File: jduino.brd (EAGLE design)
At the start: 58.1 x 66 mm, 18 parts, among them IC1 LM2936Z-5.0, IC2 ATMEGA48/88/168-PU, J1 Analog I/O, J2 Digital I/O, J3 Digital I/O, J5 Power Jumpers, J6 FTDI Jumpers, Q1 16 mHz

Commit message: Final fixes for printing.
Replaced power IC with 2931. Added an LED on pin 13.
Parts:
- added LED2: LED 13, led:LED3MM
- added R3: 330, rcl:0204/5
- IC1: value LM2936Z-5.0 -> L4931; device national-semiconductor:TO92 -> jb:TO-92
- J7: value (none) -> POWER 6 - 36V
- moved IC1 1.27 mm to (33.0, 58.4), flipped to the top, turned to 180 degrees
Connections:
- removed net D1: IC2.3, J2.2, J6.2
- new net N$4: LED2.K, R3.2
- net D13: now also LED2.A
- net GND: now also R3.1
- net RESET: now also IC2.3, J2.2, J6.2
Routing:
- net D1: track 35.9 -> 0.00 mm, vias 2 -> 0
- net RESET: track 74.6 -> 107.8 mm, vias 4 -> 6
- net GND: track 223.9 -> 234.1 mm
- net D7: track 28.1 -> 33.1 mm
- net D6: track 28.1 -> 32.6 mm
- net D5: track 28.1 -> 32.6 mm
- net +5V: track 152.1 -> 156.0 mm
- net D9: track 36.3 -> 37.5 mm
- net D8: track 27.6 -> 28.9 mm
- net D13: track 59.1 -> 60.4 mm
- net D12: track 54.0 -> 55.3 mm
- net D10: track 43.9 -> 45.2 mm
- net D11: track 49.0 -> 50.2 mm
- net N$6: track 8.15 -> 6.88 mm

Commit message: Small fixes to the circuit.
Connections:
- new net D1: IC2.3, J2.2, J6.2
- net RESET: no longer IC2.3, J2.2, J6.2
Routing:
- net RESET: track 107.8 -> 71.9 mm, vias 6 -> 4
- net D1: track 0.00 -> 35.9 mm, vias 0 -> 2
- net N$4: track 0.00 -> 2.54 mm
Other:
- board text added: "jduino v1.0"
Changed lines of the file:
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@@
 <drawing>
 <settings>
-<setting alwaysvectorfont="no"/>
+<setting alwaysvectorfont="yes"/>
 <setting verticaltext="up"/>
 </settings>
-<grid distance="0.05" unitdist="inch" unit="inch" style="lines" multiple="1" display="yes" altdistance="0.025" altunitdist="inch" altunit="inch"/>
+<grid distance="0.05" unitdist="inch" unit="mm" style="lines" multiple="1" display="yes" altdistance="0.025" altunitdist="inch" altunit="inch"/>
 <layers>
-<layer number="1" name="Top" color="4" fill="1" visible="no" active="yes"/>
+<layer number="1" name="Top" color="4" fill="1" visible="yes" active="yes"/>
 <layer number="16" name="Bottom" color="1" fill="1" visible="yes" active="yes"/>
 <layer number="17" name="Pads" color="2" fill="1" visible="yes" active="yes"/>
 <layer number="18" name="Vias" color="2" fill="1" visible="yes" active="yes"/>
-<layer number="19" name="Unrouted" color="6" fill="1" visible="no" active="yes"/>
+<layer number="19" name="Unrouted" color="6" fill="1" visible="yes" active="yes"/>
 <layer number="20" name="Dimension" color="15" fill="1" visible="yes" active="yes"/>
 <layer number="21" name="tPlace" color="16" fill="1" visible="no" active="yes"/>
@@
 <layer number="106" name="bPlate" color="7" fill="1" visible="no" active="yes"/>
 <layer number="107" name="Crop" color="7" fill="1" visible="no" active="yes"/>
-<layer number="116" name="Patch_BOT" color="9" fill="4" visible="no" active="yes"/>
+<layer number="116" name="centerDrill" color="7" fill="1" visible="yes" active="yes"/>
 <layer number="121" name="_tsilk" color="7" fill="1" visible="no" active="yes"/>
 <layer number="122" name="_bsilk" color="7" fill="1" visible="no" active="yes"/>
@@
 <wire x1="58.09" y1="66.03" x2="0" y2="66.03" width="0" layer="20"/>
 <wire x1="0" y1="66.03" x2="0" y2="0" width="0" layer="20"/>
+<text x="13.335" y="47.625" size="1.016" layer="16" ratio="10" rot="MR0">jduino v1.0</text>
 </plain>
 <attributes>
@@
 <wire x1="45.72" y1="2.54" x2="15.24" y2="2.54" width="0.6096" layer="16"/>
 <wire x1="15.24" y1="2.54" x2="7.62" y2="10.16" width="0.6096" layer="16"/>
-<polygon width="0.6096" layer="16">
+<polygon width="0.25" layer="16">
 <vertex x="1.27" y="1.27"/>
+<vertex x="57.15" y="1.27"/>
+<vertex x="57.15" y="64.77"/>
 <vertex x="1.27" y="64.77"/>
-<vertex x="57.15" y="64.77"/>
-<vertex x="57.15" y="1.27"/>
 </polygon>
 </signal>
@@
 <contactref element="RESET" pad="4"/>
 <contactref element="C4" pad="1"/>
-<contactref element="J5" pad="1"/>
 <wire x1="30.48" y1="13.97" x2="34.29" y2="13.97" width="0.4064" layer="16"/>
 <wire x1="29.21" y1="10.16" x2="30.48" y2="11.43" width="0.4064" layer="16"/>
@@
 <wire x1="12.7" y1="11.43" x2="11.43" y2="11.43" width="0.4064" layer="16"/>
 <wire x1="11.43" y1="11.43" x2="9.8806" y2="10.8712" width="0.4064" layer="16"/>
-<wire x1="29.21" y1="10.16" x2="30.48" y2="8.89" width="0.4064" layer="16"/>
-<wire x1="30.48" y1="8.89" x2="30.48" y2="7.62" width="0.4064" layer="16"/>
 <wire x1="30.48" y1="7.62" x2="22.86" y2="7.62" width="0.4064" layer="1"/>
 <wire x1="22.86" y1="7.62" x2="19.05" y2="11.43" width="0.4064" layer="16"/>
@@
 <via x="30.48" y="7.62" extent="1-16" drill="0.9" shape="square"/>
 <via x="22.86" y="7.62" extent="1-16" drill="0.9" shape="square"/>
-<contactref element="J6" pad="2"/>
-<contactref element="IC2" pad="3"/>
-<contactref element="J2" pad="2"/>
-<wire x1="30.48" y1="19.05" x2="43.18" y2="19.05" width="0.4064" layer="16"/>
-<wire x1="43.18" y1="19.05" x2="45.72" y2="19.05" width="0.4064" layer="16"/>
-<wire x1="45.72" y1="19.05" x2="48.26" y2="16.51" width="0.4064" layer="16"/>
-<wire x1="48.26" y1="16.51" x2="53.34" y2="16.51" width="0.4064" layer="16"/>
-<wire x1="41.91" y1="7.62" x2="41.91" y2="11.43" width="0.4064" layer="16"/>
-<wire x1="41.91" y1="11.43" x2="43.18" y2="12.7" width="0.4064" layer="16"/>
-<wire x1="43.18" y1="12.7" x2="43.18" y2="19.05" width="0.4064" layer="1"/>
-<via x="43.18" y="12.7" extent="1-16" drill="1" shape="square"/>
-<via x="43.18" y="19.05" extent="1-16" drill="1" shape="square"/>
-<wire x1="8.89" y1="44.45" x2="5.08" y2="44.45" width="0.4064" layer="16"/>
-<wire x1="30.48" y1="13.97" x2="30.48" y2="19.05" width="0" layer="19" extent="1-1"/>
+<wire x1="30.48" y1="7.62" x2="30.48" y2="8.89" width="0.4" layer="16"/>
+<wire x1="30.48" y1="8.89" x2="29.21" y2="10.16" width="0.4" layer="16"/>
+<contactref element="J5" pad="1"/>
+<wire x1="5.08" y1="44.45" x2="8.89" y2="44.45" width="0.4" layer="16"/>
 </signal>
 <signal name="A0">
@@
 <contactref element="J1" pad="4"/>
 <contactref element="IC2" pad="26"/>
-<wire x1="5.08" y1="19.05" x2="22.86" y2="19.05" width="0.4064" layer="16"/>
+<wire x1="5.08" y1="19.05" x2="22.86" y2="19.05" width="0.4" layer="16"/>
 </signal>
 <signal name="A4">
@@
 <contactref element="LED2" pad="K"/>
 <contactref element="R3" pad="2"/>
-<wire x1="39.37" y1="54.61" x2="41.91" y2="54.61" width="0" layer="19" extent="1-1"/>
+<wire x1="39.37" y1="54.61" x2="41.91" y2="54.61" width="0.4" layer="16"/>
+</signal>
+<signal name="D1">
+<contactref element="J6" pad="2"/>
+<contactref element="IC2" pad="3"/>
+<contactref element="J2" pad="2"/>
+<wire x1="30.48" y1="19.05" x2="43.18" y2="19.05" width="0.4064" layer="16"/>
+<wire x1="43.18" y1="19.05" x2="45.72" y2="19.05" width="0.4064" layer="16"/>
+<wire x1="45.72" y1="19.05" x2="48.26" y2="16.51" width="0.4064" layer="16"/>
+<wire x1="48.26" y1="16.51" x2="53.34" y2="16.51" width="0.4064" layer="16"/>
+<wire x1="41.91" y1="7.62" x2="41.91" y2="11.43" width="0.4064" layer="16"/>
+<wire x1="41.91" y1="11.43" x2="43.18" y2="12.7" width="0.4064" layer="16"/>
+<wire x1="43.18" y1="12.7" x2="43.18" y2="19.05" width="0.4064" layer="1"/>
+<via x="43.18" y="12.7" extent="1-16" drill="1" shape="square"/>
+<via x="43.18" y="19.05" extent="1-16" drill="1" shape="square"/>
 </signal>
 </signals>

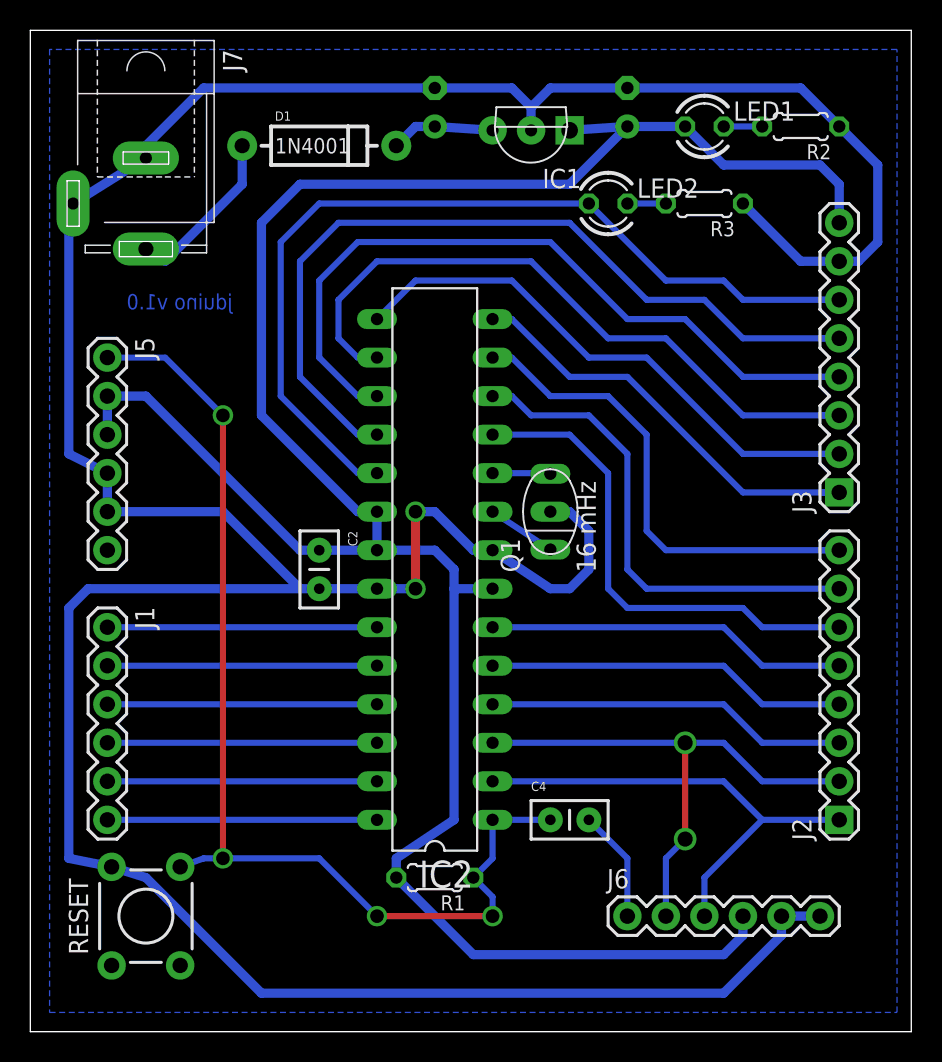
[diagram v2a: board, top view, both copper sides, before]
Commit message: Cleaned up area around reset button.
Rotated the reset button. Tied extra button terminals to the live
terminals.
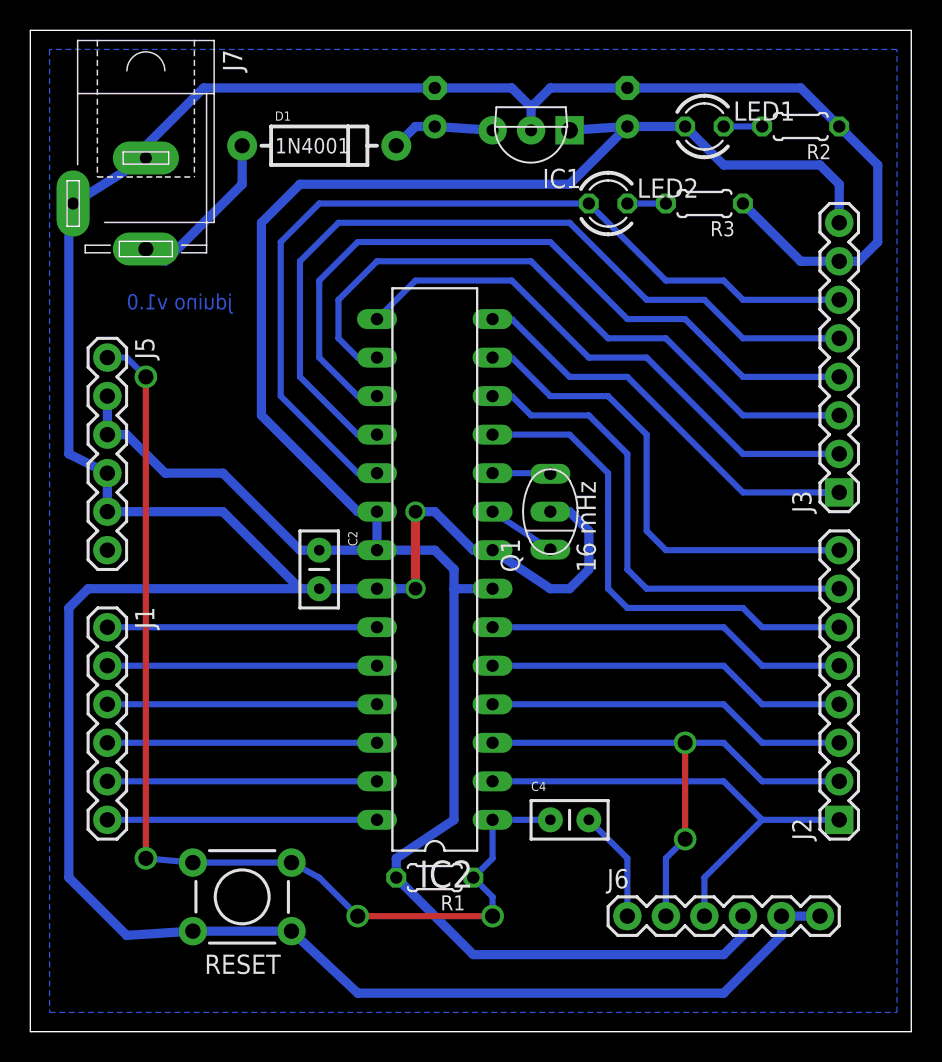
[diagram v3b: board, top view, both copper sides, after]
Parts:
- moved RESET 6.48 mm to (14.0, 8.89), turned to 180 degrees
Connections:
- net GND: now also RESET.1
- net RESET: now also RESET.3
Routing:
- net RESET: track 71.9 -> 70.2 mm
- net GND: track 234.1 -> 235.2 mm
- net +5V: track 156.0 -> 154.9 mm
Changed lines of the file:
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@@
 <setting verticaltext="up"/>
 </settings>
-<grid distance="0.05" unitdist="inch" unit="mm" style="lines" multiple="1" display="yes" altdistance="0.025" altunitdist="inch" altunit="inch"/>
+<grid distance="50" unitdist="mil" unit="mil" style="lines" multiple="1" display="yes" altdistance="25" altunitdist="mil" altunit="mil"/>
 <layers>
 <layer number="1" name="Top" color="4" fill="1" visible="yes" active="yes"/>
@@
 <layer number="19" name="Unrouted" color="6" fill="1" visible="yes" active="yes"/>
 <layer number="20" name="Dimension" color="15" fill="1" visible="yes" active="yes"/>
-<layer number="21" name="tPlace" color="16" fill="1" visible="no" active="yes"/>
+<layer number="21" name="tPlace" color="16" fill="1" visible="yes" active="yes"/>
 <layer number="22" name="bPlace" color="14" fill="1" visible="no" active="yes"/>
-<layer number="23" name="tOrigins" color="15" fill="1" visible="no" active="yes"/>
+<layer number="23" name="tOrigins" color="15" fill="1" visible="yes" active="yes"/>
 <layer number="24" name="bOrigins" color="15" fill="1" visible="no" active="yes"/>
 <layer number="25" name="tNames" color="7" fill="1" visible="no" active="yes"/>
@@
 <element name="C1" library="rcl" package="E2,5-6" value="220uf 10v" x="39.37" y="60.96" rot="MR90"/>
 <element name="IC2" library="atmega8" package="DIL28-3" value="ATMEGA48/88/168-PU" x="26.67" y="30.48" rot="R90"/>
-<element name="RESET" library="SparkFun" package="TACTILE-PTH" value="5501" x="7.62" y="7.62" rot="R90"/>
+<element name="RESET" library="SparkFun" package="TACTILE-PTH" value="5501" x="13.97" y="8.89" rot="R180"/>
 <element name="R1" library="rcl" package="0204/5" value="10K" x="26.67" y="10.16" rot="R180"/>
 <element name="Q1" library="murata-resonators" package="CSTLS_X" value="16 mHz" x="34.29" y="34.29" rot="R90"/>
@@
 <wire x1="17.78" y1="29.21" x2="19.05" y2="29.21" width="0.6096" layer="16"/>
 <wire x1="52.07" y1="7.62" x2="49.53" y2="7.62" width="0.6096" layer="16"/>
-<wire x1="49.53" y1="7.62" x2="49.53" y2="6.35" width="0.6096" layer="16"/>
-<wire x1="7.62" y1="10.16" x2="5.3594" y2="10.8712" width="0.6096" layer="16"/>
-<wire x1="45.72" y1="2.54" x2="49.53" y2="6.35" width="0.6096" layer="16"/>
 <wire x1="17.78" y1="29.21" x2="3.81" y2="29.21" width="0.6096" layer="16"/>
 <wire x1="3.81" y1="29.21" x2="2.54" y2="27.94" width="0.6096" layer="16"/>
-<wire x1="2.54" y1="27.94" x2="2.54" y2="11.43" width="0.6096" layer="16"/>
-<wire x1="2.54" y1="11.43" x2="5.3594" y2="10.8712" width="0.6096" layer="16"/>
 <wire x1="2.54" y1="38.1" x2="5.08" y2="36.83" width="0.6096" layer="16"/>
 <wire x1="30.48" y1="31.75" x2="29.21" y2="31.75" width="0.6096" layer="16"/>
@@
 <wire x1="53.34" y1="50.8" x2="50.8" y2="50.8" width="0.6096" layer="16"/>
 <wire x1="50.8" y1="50.8" x2="46.99" y2="54.61" width="0.6096" layer="16"/>
-<wire x1="45.72" y1="2.54" x2="15.24" y2="2.54" width="0.6096" layer="16"/>
-<wire x1="15.24" y1="2.54" x2="7.62" y2="10.16" width="0.6096" layer="16"/>
-<polygon width="0.25" layer="16">
+<wire x1="2.54" y1="27.94" x2="2.54" y2="10.16" width="0.6096" layer="16"/>
+<contactref element="RESET" pad="1"/>
+<wire x1="6.35" y1="6.35" x2="2.54" y2="10.16" width="0.6096" layer="16"/>
+<wire x1="6.35" y1="6.35" x2="10.7188" y2="6.6294" width="0.6096" layer="16"/>
+<wire x1="10.7188" y1="6.6294" x2="17.2212" y2="6.6294" width="0.6096" layer="16"/>
+<wire x1="49.53" y1="7.62" x2="49.53" y2="6.35" width="0.6096" layer="16"/>
+<wire x1="49.53" y1="6.35" x2="45.72" y2="2.54" width="0.6096" layer="16"/>
+<wire x1="45.72" y1="2.54" x2="21.59" y2="2.54" width="0.6096" layer="16"/>
+<wire x1="21.59" y1="2.54" x2="17.2212" y2="6.6294" width="0.6096" layer="16"/>
+<polygon width="0.4064" layer="16">
+<vertex x="1.27" y="64.77"/>
 <vertex x="1.27" y="1.27"/>
 <vertex x="57.15" y="1.27"/>
 <vertex x="57.15" y="64.77"/>
-<vertex x="1.27" y="64.77"/>
 </polygon>
 </signal>
@@
 <contactref element="J3" pad="8"/>
 <contactref element="C2" pad="1"/>
-<wire x1="5.08" y1="41.91" x2="5.08" y2="39.37" width="0.6096" layer="16"/>
 <wire x1="22.86" y1="34.29" x2="22.86" y2="31.75" width="0.6096" layer="16"/>
 <wire x1="22.86" y1="31.75" x2="19.05" y2="31.75" width="0.6096" layer="16"/>
-<wire x1="5.08" y1="41.91" x2="7.62" y2="41.91" width="0.6096" layer="16"/>
-<wire x1="7.62" y1="41.91" x2="17.78" y2="31.75" width="0.6096" layer="16"/>
-<wire x1="17.78" y1="31.75" x2="19.05" y2="31.75" width="0.6096" layer="16"/>
 <wire x1="22.86" y1="34.29" x2="21.59" y2="34.29" width="0.6096" layer="16"/>
 <wire x1="21.59" y1="34.29" x2="15.24" y2="40.64" width="0.6096" layer="16"/>
@@
 <wire x1="52.07" y1="57.15" x2="45.72" y2="57.15" width="0.6096" layer="16"/>
 <wire x1="35.56" y1="59.436" x2="39.37" y2="59.69" width="0.6096" layer="16"/>
+<wire x1="5.08" y1="39.37" x2="6.35" y2="39.37" width="0.6096" layer="16"/>
+<wire x1="6.35" y1="39.37" x2="8.89" y2="36.83" width="0.6096" layer="16"/>
+<wire x1="8.89" y1="36.83" x2="12.7" y2="36.83" width="0.6096" layer="16"/>
+<wire x1="12.7" y1="36.83" x2="17.78" y2="31.75" width="0.6096" layer="16"/>
+<wire x1="17.78" y1="31.75" x2="19.05" y2="31.75" width="0.6096" layer="16"/>
+<wire x1="5.08" y1="41.91" x2="5.08" y2="39.37" width="0.6096" layer="16"/>
 </signal>
 <signal name="N$5">
@@
 <wire x1="29.21" y1="10.16" x2="30.48" y2="11.43" width="0.4064" layer="16"/>
 <wire x1="30.48" y1="11.43" x2="30.48" y2="13.97" width="0.4064" layer="16"/>
-<wire x1="8.89" y1="44.45" x2="12.7" y2="40.64" width="0.4064" layer="16"/>
-<wire x1="12.7" y1="40.64" x2="12.7" y2="11.43" width="0.4064" layer="1"/>
-<wire x1="12.7" y1="11.43" x2="11.43" y2="11.43" width="0.4064" layer="16"/>
-<wire x1="11.43" y1="11.43" x2="9.8806" y2="10.8712" width="0.4064" layer="16"/>
-<wire x1="30.48" y1="7.62" x2="22.86" y2="7.62" width="0.4064" layer="1"/>
-<wire x1="22.86" y1="7.62" x2="19.05" y2="11.43" width="0.4064" layer="16"/>
-<wire x1="19.05" y1="11.43" x2="12.7" y2="11.43" width="0.4064" layer="16"/>
-<via x="12.7" y="40.64" extent="1-16" drill="0.9" shape="square"/>
-<via x="12.7" y="11.43" extent="1-16" drill="0.9" shape="square"/>
-<via x="30.48" y="7.62" extent="1-16" drill="0.9" shape="square"/>
-<via x="22.86" y="7.62" extent="1-16" drill="0.9" shape="square"/>
-<wire x1="30.48" y1="7.62" x2="30.48" y2="8.89" width="0.4" layer="16"/>
-<wire x1="30.48" y1="8.89" x2="29.21" y2="10.16" width="0.4" layer="16"/>
 <contactref element="J5" pad="1"/>
-<wire x1="5.08" y1="44.45" x2="8.89" y2="44.45" width="0.4" layer="16"/>
+<contactref element="RESET" pad="3"/>
+<wire x1="17.2212" y1="11.1506" x2="19.05" y2="10.16" width="0.4064" layer="16"/>
+<wire x1="19.05" y1="10.16" x2="21.59" y2="7.62" width="0.4064" layer="16"/>
+<wire x1="29.21" y1="10.16" x2="30.48" y2="8.89" width="0.4064" layer="16"/>
+<wire x1="30.48" y1="8.89" x2="30.48" y2="7.62" width="0.4064" layer="16"/>
+<wire x1="21.59" y1="7.62" x2="30.48" y2="7.62" width="0.4064" layer="1"/>
+<via x="21.59" y="7.62" extent="1-16" drill="1" shape="square"/>
+<via x="30.48" y="7.62" extent="1-16" drill="1" shape="square"/>
+<wire x1="5.08" y1="44.45" x2="6.35" y2="44.45" width="0.4064" layer="16"/>
+<wire x1="6.35" y1="44.45" x2="7.62" y2="43.18" width="0.4064" layer="16"/>
+<wire x1="7.62" y1="43.18" x2="7.62" y2="11.43" width="0.4064" layer="1"/>
+<wire x1="7.62" y1="11.43" x2="10.7188" y2="11.1506" width="0.4064" layer="16"/>
+<wire x1="10.7188" y1="11.1506" x2="17.2212" y2="11.1506" width="0.4064" layer="16"/>
+<via x="7.62" y="43.18" extent="1-16" drill="1" shape="square"/>
+<via x="7.62" y="11.43" extent="1-16" drill="1" shape="square"/>
 </signal>
 <signal name="A0">
@@
 <contactref element="J1" pad="4"/>
 <contactref element="IC2" pad="26"/>
-<wire x1="5.08" y1="19.05" x2="22.86" y2="19.05" width="0.4" layer="16"/>
+<wire x1="5.08" y1="19.05" x2="22.86" y2="19.05" width="0.4064" layer="16"/>
 </signal>
 <signal name="A4">
@@
 <contactref element="LED2" pad="K"/>
 <contactref element="R3" pad="2"/>
-<wire x1="39.37" y1="54.61" x2="41.91" y2="54.61" width="0.4" layer="16"/>
+<wire x1="39.37" y1="54.61" x2="41.91" y2="54.61" width="0.4064" layer="16"/>
 </signal>
 <signal name="D1">
@@
 </signal>
 </signals>
+<errors>
+</errors>
 </board>
 </drawing>
